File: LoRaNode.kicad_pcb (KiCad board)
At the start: 2 copper layers, 43 x 93 mm, 59 parts, among them J10 D4, J11 A1, J12 A2, J13 A3, J14 D8, J2 Conn_01x06, J3 Conn_01x02, J4 ISP, J5 Conn_01x06, J6 Conn_01x04, J7 USB_B_Micro, J8 D2, J9 D3, U1 RFM95W-868S2, U2 MCP73871, U3 TPS63031, U4 ATMEGA328P-AU, Y1 8MHz HC5032/4

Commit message: v0.1
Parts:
- removed C10, C4, C5, C6, C7, C9: 10u, Capacitors_SMD:C_0805
- removed C3: 4700uF/10V, Capacitors_THT:CP_Radial_D12.5mm_P25mm
- removed C8: 100n, Capacitors_SMD:C_0603
- removed D1: MBR120VLSFT1G, Capacitors_SMD:C_0805
- removed D2: CHRG, LEDs:LED_0805
- removed D3: DONE, LEDs:LED_0805
- removed D4: PWR, LEDs:LED_0805
- removed J3: Conn_01x02, Pin_Headers:Pin_Header_Straight_1x02_Pitch2.54mm
- removed J7: USB_B_Micro, Connector_USB:USB_Micro-B_Molex-105017-0001
- removed L2: 1u5, Inductors:Inductor_Wurth_MAPI-3012
- removed R1, R2, R3: 1k, Resistors_SMD:R_0603
- removed R10: 69k8, Resistors_SMD:R_0603
- removed R4: 270k, Resistors_SMD:R_0603
- removed R5, R7: 100k, Resistors_SMD:R_0603
- removed R6: 2k, Resistors_SMD:R_0603
- removed R8: 1k54, Resistors_SMD:R_0603
- removed R9: THERM 10k, Resistors_SMD:R_0805
- removed U2: MCP73871, Housings_DFN_QFN:QFN-20-1EP_4x4mm_Pitch0.5mm
- removed U3: TPS63031, Package_SON:Texas_S-PWSON-N10
- added G***: LoRa-Logo-Small, kicad-footprints-master:LoRa-Logo-Small, F.Cu at (150.1, 93.7)
- added G***: RiskeLogo, kicad-footprints-master:RiskeLogo, B.Cu at (136.0, 94.7)
- added J1: A3, TestPoint:TestPoint_Pad_D1.0mm, F.Cu at (156.0, 113.7)
- added openhw: , kicad-footprints-master:openhw, B.Cu at (142.4, 106.4)
- C1: value 2p7 -> dnp
- J2: value Conn_01x06 -> Conn_01x03; footprint Pin_Headers:Pin_Header_Straight_1x06_Pitch2.54mm -> Connector_PinHeader_2.54mm:PinHeader_1x03_P2.54mm_Vertical
- L1: value 1n8 -> 0R
- moved C2 21.6 mm to (133.8, 88.7), turned to 180 degrees
- moved L1 19.0 mm to (136.2, 89.9), turned to 180 degrees
- moved C13 18.8 mm to (132.0, 91.8), turned to 180 degrees
- moved C14 18.4 mm to (132.3, 93.5), turned to 180 degrees
- moved U1 17.0 mm to (135.0, 103.8)
- moved C1 16.5 mm to (137.4, 88.7)
- moved J2 15.3 mm to (164.0, 116.2), turned to 90 degrees
- moved C11 15.0 mm to (163.4, 98.8)
- moved C12 15.0 mm to (154.5, 109.2)
- moved C15 15.0 mm to (165.4, 100.8)
- moved C16 15.0 mm to (153.5, 108.2)
- moved C17 15.0 mm to (167.0, 98.5)
- moved C18 15.0 mm to (157.3, 97.5)
- moved C19 15.0 mm to (163.1, 95.2)
- moved C20 15.0 mm to (166.0, 108.3)
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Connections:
- C1 pad 2: Earth -> GND
- C11 pad 2: Earth -> GND
- C12 pad 2: Earth -> GND
- C13 pad 2: Earth -> GND
- C14 pad 2: Earth -> GND
- C15 pad 2: Earth -> GND
- C16 pad 2: Earth -> GND
- C17 pad 2: Earth -> GND
- C18 pad 2: Earth -> GND
- C19 pad 2: Earth -> GND
- C2 pad 2: Earth -> GND
- J2 pad 1: Earth -> GND
- J2 pad 3: Earth -> GND
- J4 pad 6: Earth -> GND
- J5 pad 1: Earth -> GND
- J5 pad 2: Earth -> GND
- J6 pad 1: Earth -> GND
- R17 pad 2: Earth -> GND
- U1 pad 1: Earth -> GND
- U1 pad 10: Earth -> GND
- U1 pad 8: Earth -> GND
- U4 pad 21: Earth -> GND
- U4 pad 3: Earth -> GND
- U4 pad 5: Earth -> GND
- Y1 pad 2: Earth -> GND
- Y1 pad 4: Earth -> GND
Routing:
- net Earth: track 212.7 -> 0.00 mm, vias 61 -> 0
- net GND: track 0.00 -> 185.3 mm, vias 0 -> 139
- net /ANT: track 133.8 -> 0.00 mm, vias 131 -> 0
- net VCC: track 73.1 -> 0.00 mm
- net /VBAT: track 49.7 -> 2.00 mm, vias 6 -> 0
- net /VOUT: track 18.7 -> 0.00 mm
- net /12(**/MOSI): track 33.6 -> 49.5 mm
- net +3V3: track 139.1 -> 124.4 mm
- net /D7: track 23.7 -> 34.6 mm
- net /D6: track 22.0 -> 32.9 mm
- net /D5: track 20.4 -> 31.1 mm
- net /RES: track 28.6 -> 19.0 mm, vias 2 -> 1
- net /10(**/SS): track 19.8 -> 26.6 mm
- net Net-(C1-Pad1): track 3.45 -> 9.83 mm
- net /D9: track 20.5 -> 26.7 mm
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- added copper zone on B.Cu, net GND
- added copper zone on F.Cu, net GND
- removed copper zone on F.Cu, net +3V3
- removed copper zone on B.Cu, net /ANT
- removed copper zone on F.Cu, net /VBAT
- removed copper zone on F.Cu, net /VOUT
- removed copper zone on B.Cu, net Earth
- removed copper zone on F.Cu, net Earth
- removed copper zone on F.Cu, net Net-(L2-Pad1)
- removed copper zone on F.Cu, net Net-(L2-Pad2)
- removed copper zone on F.Cu, net VCC
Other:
- board size 43 x 93 mm -> 45 x 53 mm
- net class Default: clearance 0.1 -> 0.25
- rule trace_clearance: 0.1 -> 0.25
- board text added: "GND 3V3 GND"
- board text added: "GND CTS 3V3 RX TX DTR"
- board text added: "I2C"
- board text added: "LoRa Node rev.1"
- board text added: "Vin"
- board text removed: "+ -"
- board text removed: "6V Solar panel"
- board text removed: "G 3V3 G Vin G B"
- board text removed: "GND - 3V3 RX TX RES"
- board text removed: "GND 3V3 GND VIN-6Vmax GND VBAT"

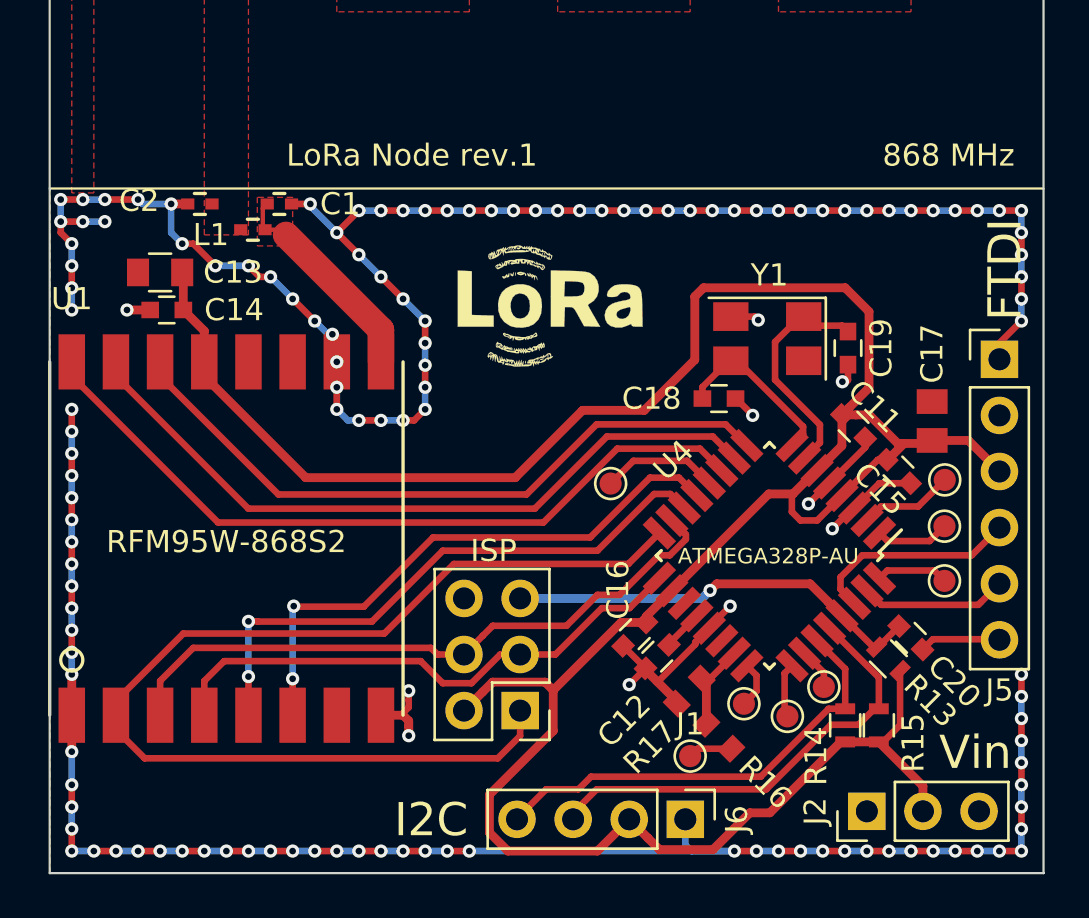
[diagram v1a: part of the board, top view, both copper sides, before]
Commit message: Moved I2C and Power connectors, Added antenna test pads, ERC done, DRC done
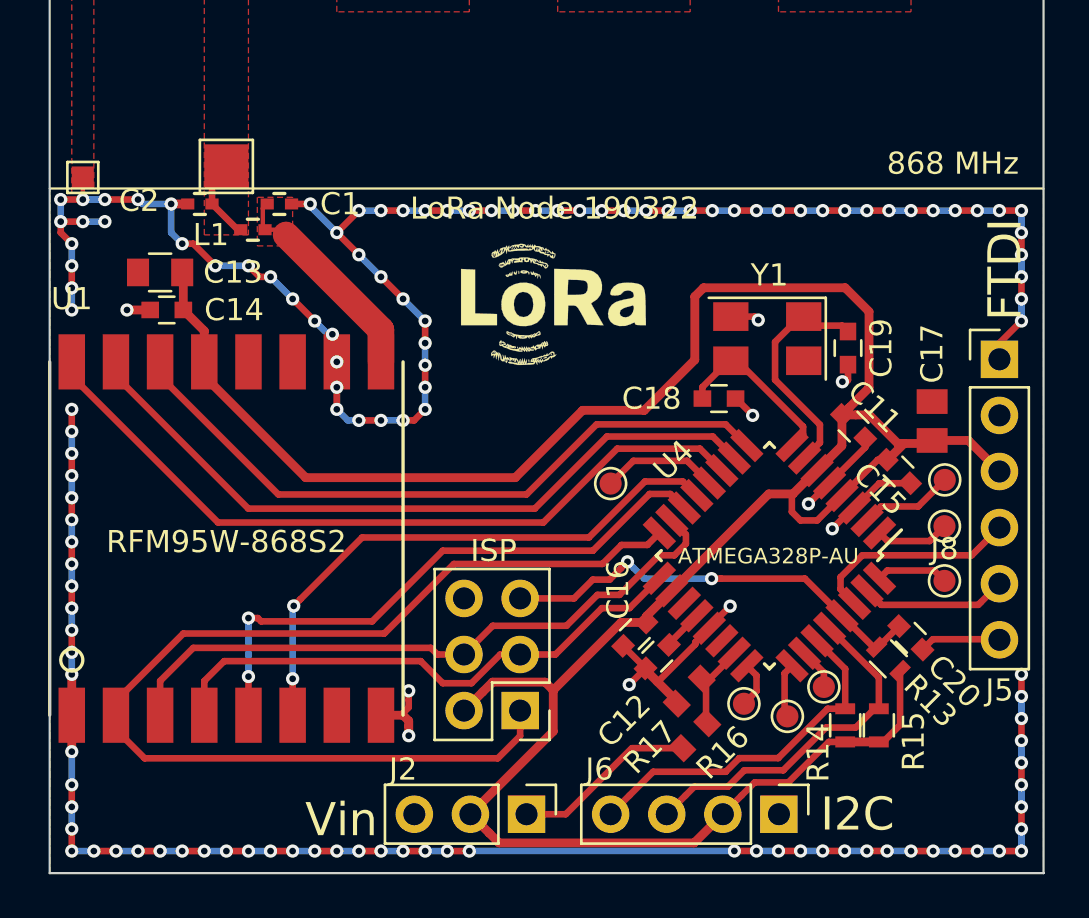
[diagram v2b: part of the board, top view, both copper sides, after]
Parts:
- removed openhw: , kicad-footprints-master:openhw
- added J3: D2, TestPoint:TestPoint_Pad_1.0x1.0mm, F.Cu at (128.5, 87.5)
- J1: value A3 -> D2; footprint TestPoint:TestPoint_Pad_D1.0mm -> TestPoint:TestPoint_Pad_2.0x2.0mm
- moved J1 34.0 mm to (135.0, 87.0)
- moved J2 15.4 mm to (148.6, 116.3), turned to 270 degrees
- moved J6 4.25 mm to (160.0, 116.3)
- moved R16 1.09 mm to (156.2, 112.8), turned to 45 degrees
- moved G*** 0.81 mm to (135.6, 94.0)
- moved G*** 0.17 mm to (150.2, 93.6)
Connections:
- C2 pad 1: /ANT -> GND
- J1 pad 1: /VBAT -> GND
- J2 pad 1: GND -> /VBAT
- L1 pad 2: /ANT -> GND
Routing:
- net /VBAT: track 2.00 -> 8.29 mm
- net +3V3: track 124.4 -> 119.7 mm
- net /SDA: track 20.7 -> 16.4 mm
- net /SCL: track 20.4 -> 16.2 mm
- net GND: track 185.3 -> 186.6 mm
- net /RES: track 19.0 -> 19.8 mm, vias 1 -> 2
- removed copper zone on F.Cu, net /ANT
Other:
- board text added: "G + G"
- board text added: "LoRa Node 190321"
- board text added: "LoRa Node 190322"
- board text removed: "GND 3V3 GND"
- board text removed: "LoRa Node rev.1"

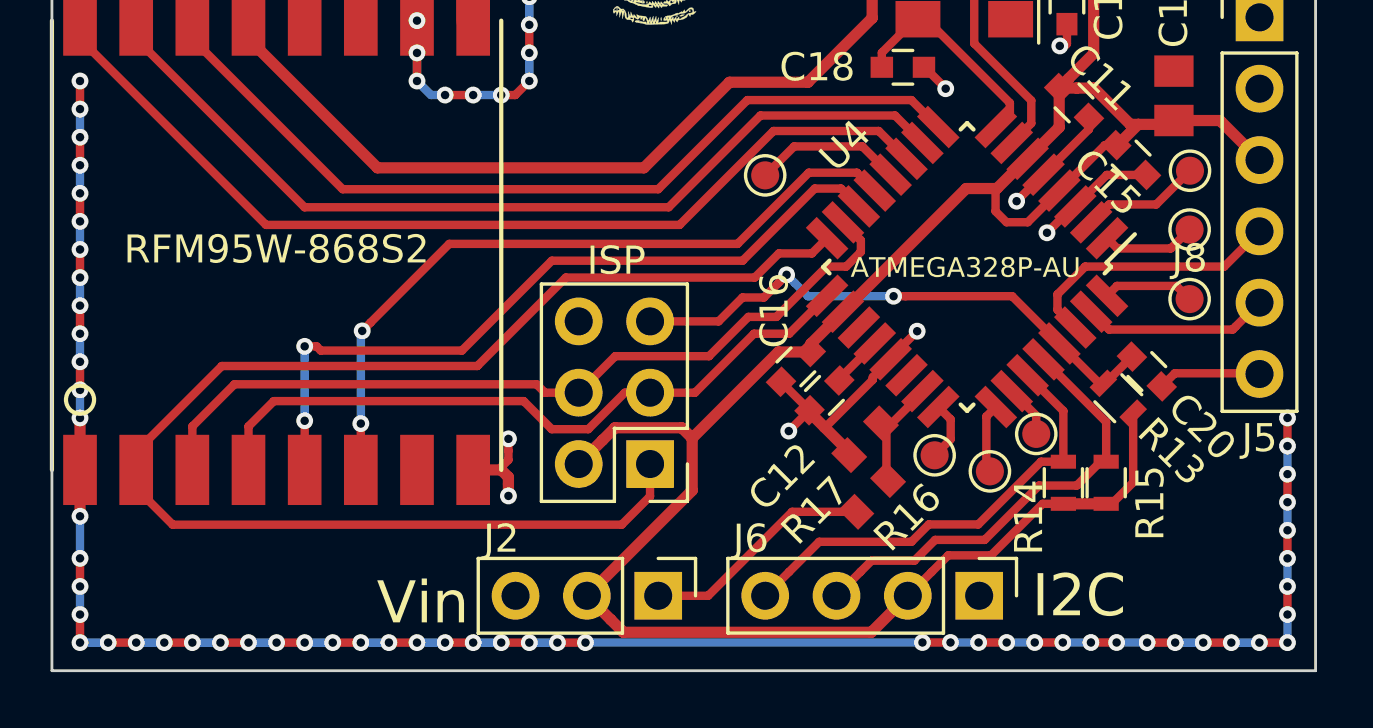
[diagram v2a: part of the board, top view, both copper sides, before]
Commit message: Changed I2C pinout
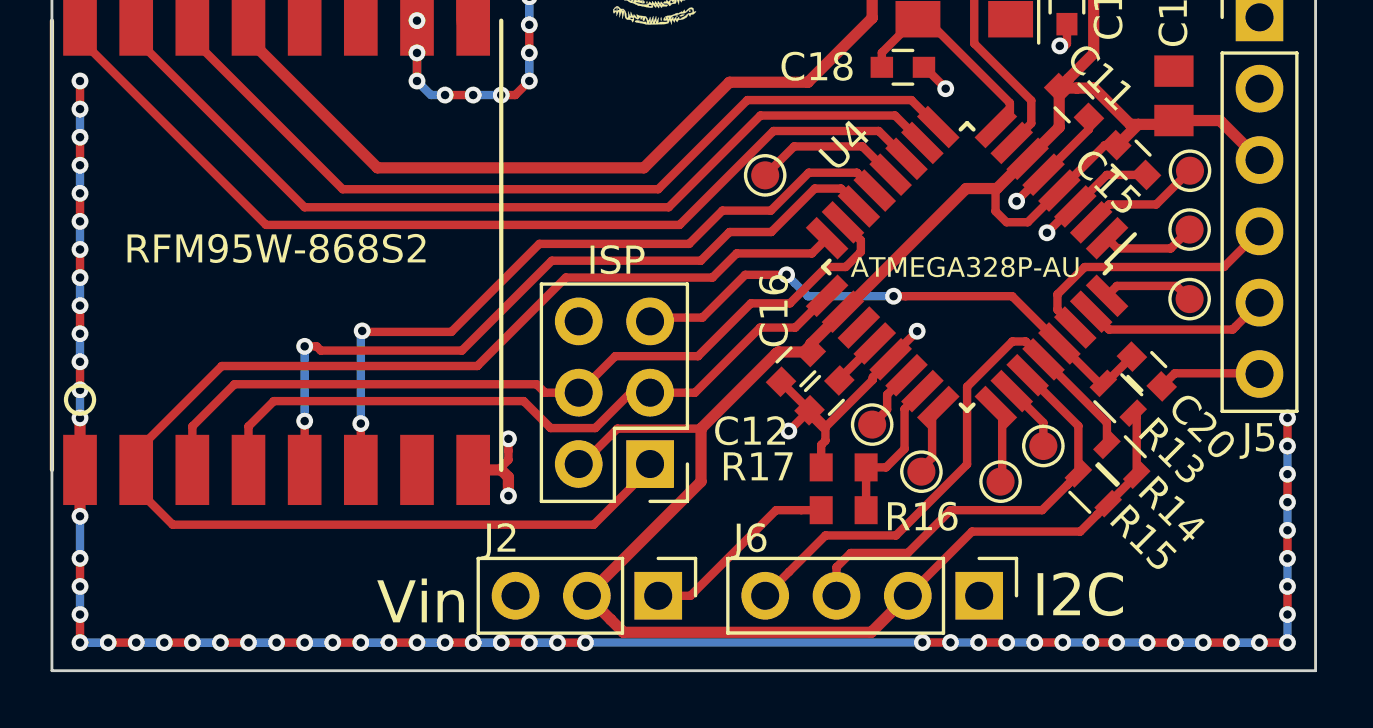
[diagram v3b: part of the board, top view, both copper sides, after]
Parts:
- added J7: A3, TestPoint:TestPoint_Pad_D1.0mm, F.Cu at (156.2, 110.2)
- moved R14 2.23 mm to (165.1, 111.5), turned to 135 degrees
- moved R17 1.26 mm to (155.2, 111.8), turned to 180 degrees
- moved R16 1.14 mm to (155.2, 113.3), turned to 0 degrees
- moved J11 0.75 mm to (158.0, 111.9)
- moved J12 0.53 mm to (160.8, 112.3)
- moved R15 0.51 mm to (164.1, 112.5), turned to 135 degrees
- moved J13 0.50 mm to (162.3, 111.0)
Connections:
- J6 pad 3: /SCL -> /SDA
- J6 pad 4: /SDA -> /SCL
- R14 pad 2: /SDA -> /SCL
- R15 pad 2: /SCL -> /SDA
- U4 pad 22: (no net) -> /A7
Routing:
- net /SCL: track 16.2 -> 19.5 mm
- net /A7: track 0.00 -> 2.26 mm
- net /A0: track 4.14 -> 5.49 mm
- net /VBAT: track 8.29 -> 7.07 mm
- net /SDA: track 16.4 -> 15.3 mm
- net /12(**/MOSI): track 49.5 -> 48.9 mm
- net /A3: track 1.89 -> 2.42 mm
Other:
- net class Default: clearance 0.25 -> 0.2
- rule trace_clearance: 0.25 -> 0.2

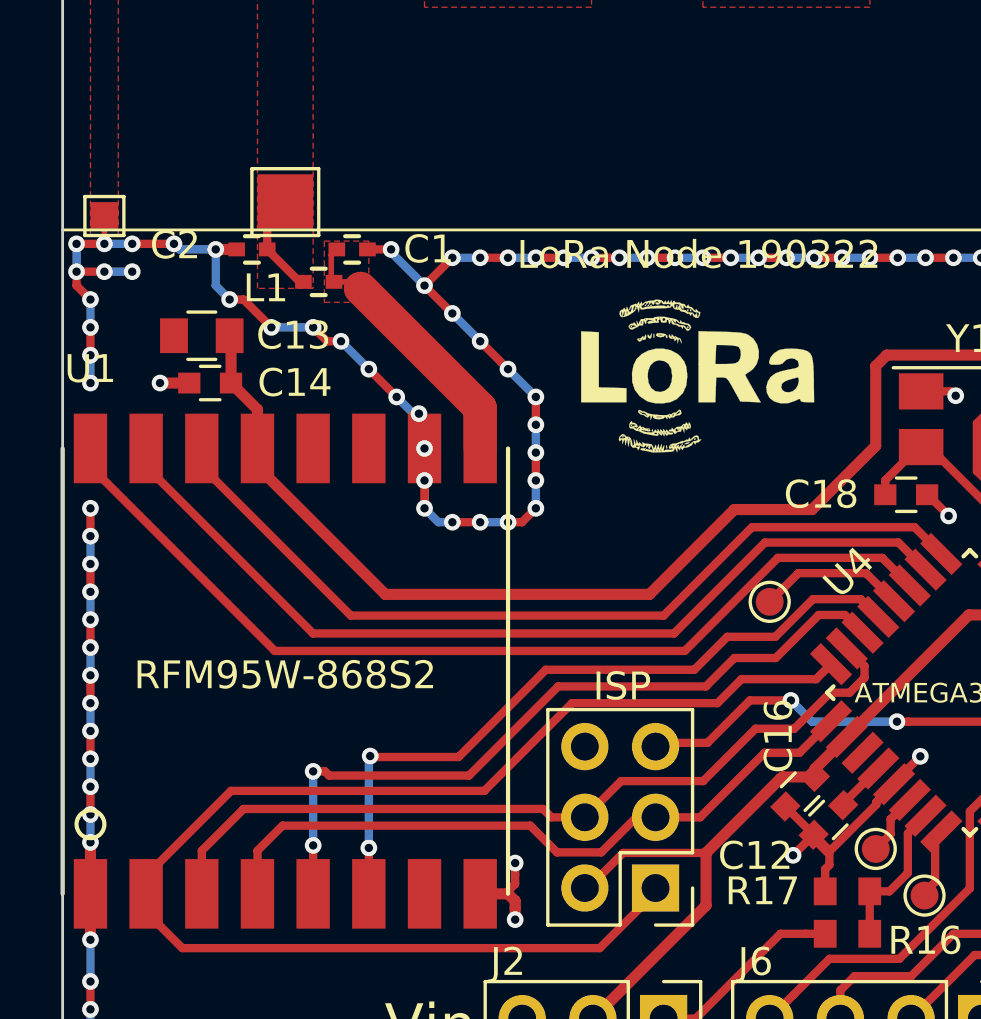
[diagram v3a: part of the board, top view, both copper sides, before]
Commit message: Silkscreen correction, removed antenna testing pads
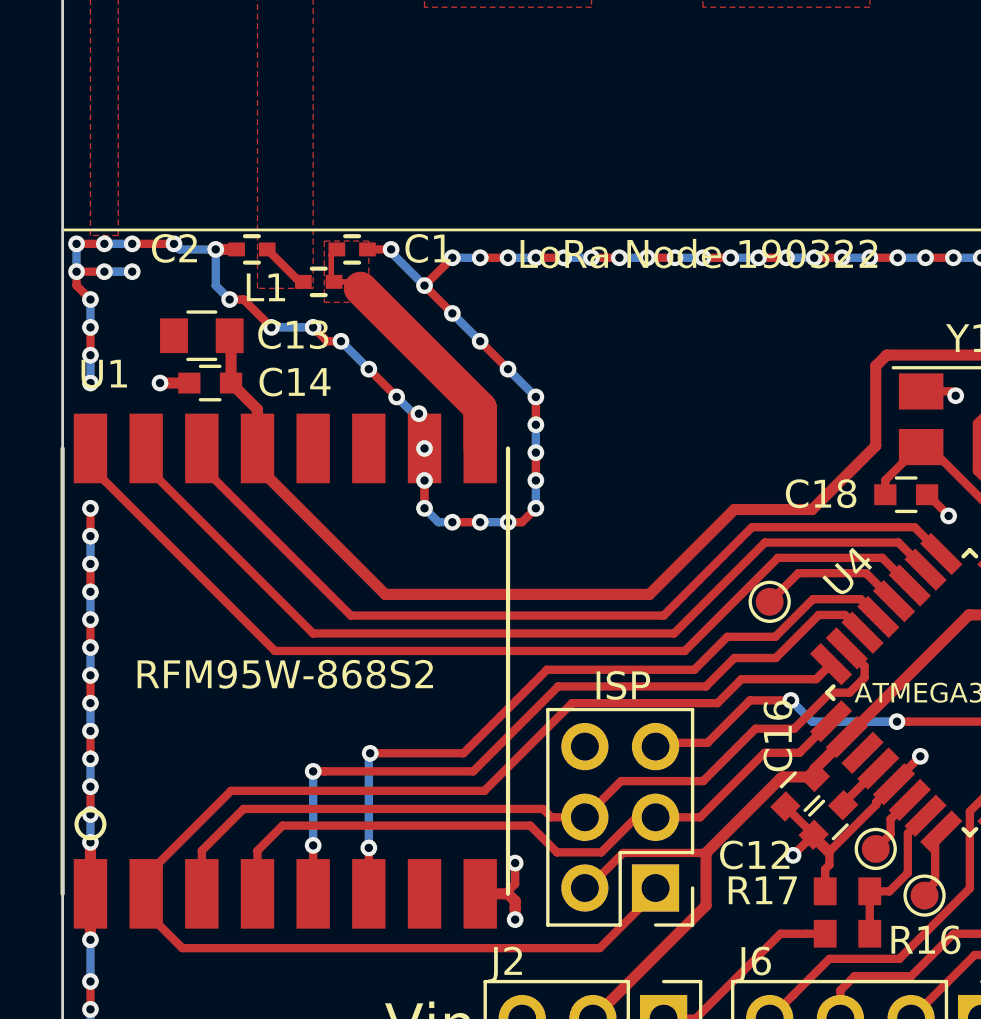
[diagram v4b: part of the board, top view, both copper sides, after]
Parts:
- removed G***: LoRa-Logo-Small, kicad-footprints-master:LoRa-Logo-Small
- removed G***: RiskeLogo, kicad-footprints-master:RiskeLogo
- removed J1: D2, TestPoint:TestPoint_Pad_2.0x2.0mm
- removed J3: D2, TestPoint:TestPoint_Pad_1.0x1.0mm
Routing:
- net GND: track 187.1 -> 184.1 mm
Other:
- board text added: "G + B"
- board text added: "SCL SDA 3V3 GND"
- board text removed: "G + G"
- board text removed: "LoRa Node 190321"
- board text removed: "SDA SCL 3V3 GND"
